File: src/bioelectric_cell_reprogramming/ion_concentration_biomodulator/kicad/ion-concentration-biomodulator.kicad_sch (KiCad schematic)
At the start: 52 parts, among them J1 532610671, J10 39-53-2045, J11 Conn_01x14_Pin, J12 Conn_01x14_Pin, J13 39-53-2045, J14 39-53-2045, J15 Conn_ARM_SWD_TagConnect_TC2030, J16 IPL1-104-01-L-D-K, J17 Conn_01x02_Pin, J18 EJ508A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

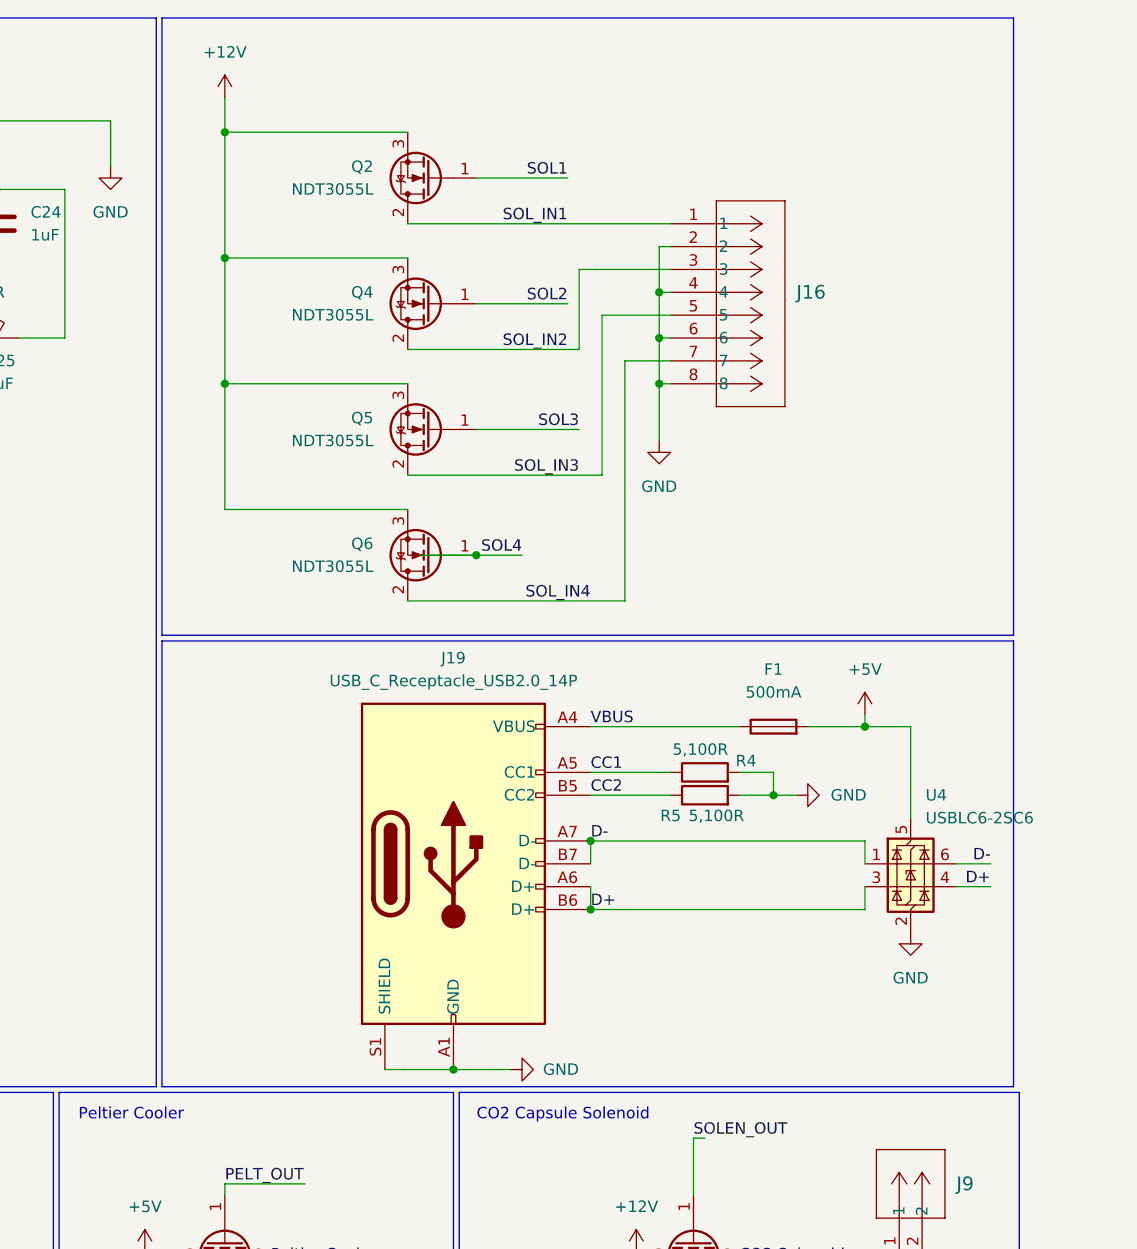
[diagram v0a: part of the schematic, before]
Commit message: fix: replaced the USB connector with one in the JLCPCB parts library
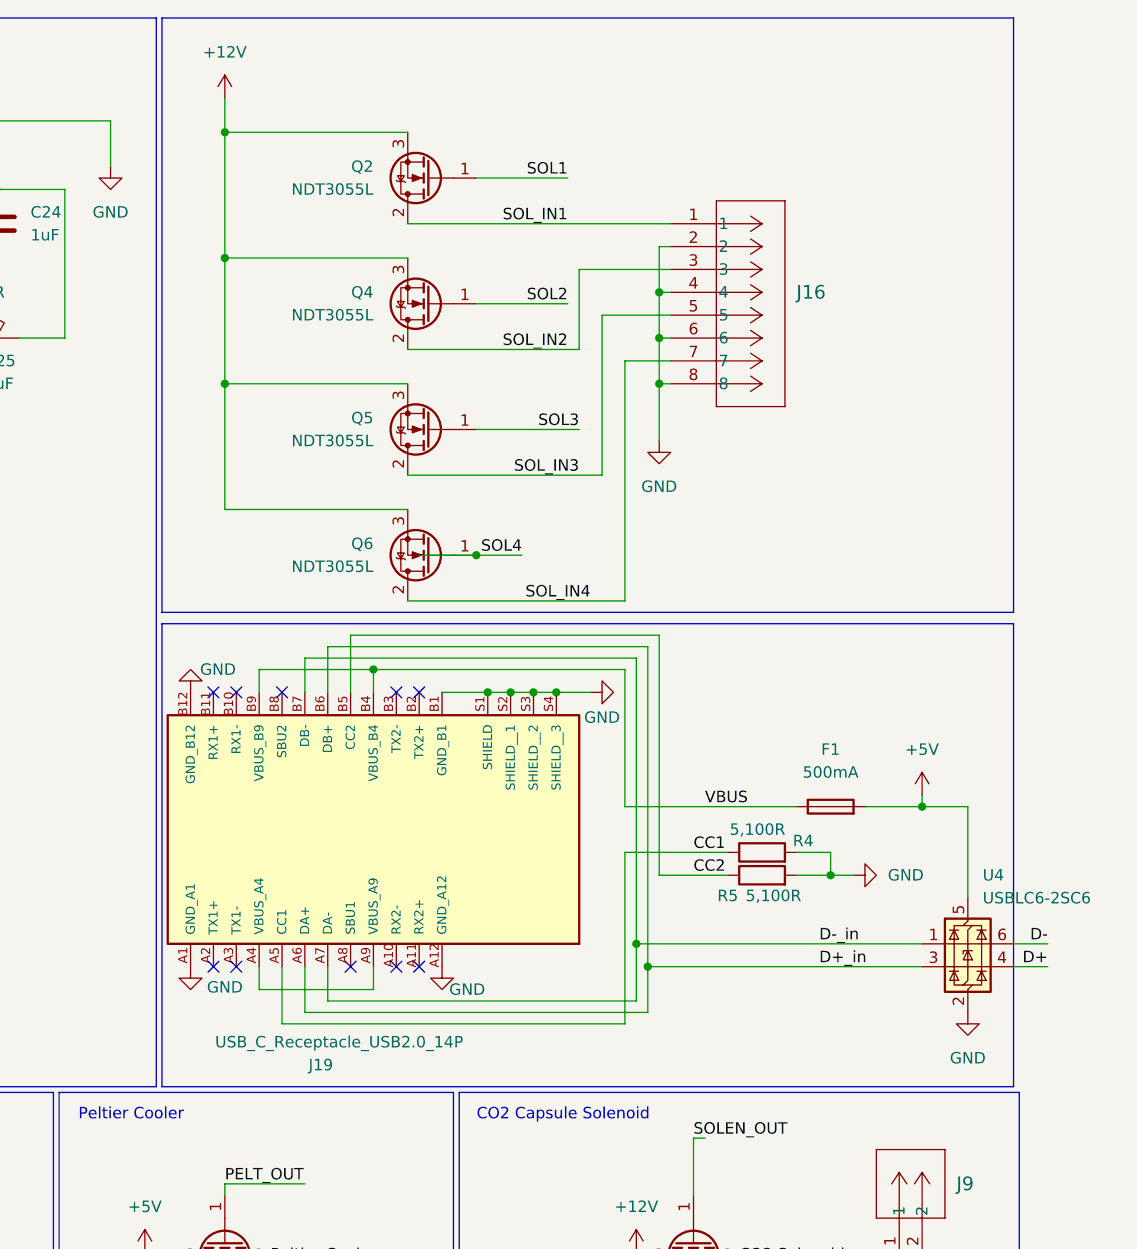
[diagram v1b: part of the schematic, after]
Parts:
- J19: footprint Connector_USB:USB_C_Receptacle_GCT_USB4105-xx-A_16P_TopMnt_Horizontal -> 12401610E4_2A:AMPHENOL_12401610E4_2A; symbol Connector:USB_C_Receptacle_USB2.0_14P -> 12401610E4_2A:12401610E4_2A; MANUFACTURER (none) -> Amphenol; MAXIMUM_PACKAGE_HEIGHT (none) -> 3.43 mm; PARTREV (none) -> C; SNAPEDA_PN (none) -> 12401610E4#2A; STANDARD (none) -> Manufacturer Recommendations
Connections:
- net D+: no longer J19.A6 (D+), J19.B6 (D+), U4.3 (I/O2)
- net D-: no longer J19.A7 (D-), J19.B7 (D-), U4.1 (I/O1)
- net GND: now also J19.S2 (SHIELD__1), J19.S3 (SHIELD__2), J19.S4 (SHIELD__3)
- net VBUS: no longer J19.A4 (VBUS), J19.A9 (VBUS)
- new net: J19.A4 (VBUS_A4), J19.A9 (VBUS_A9)
- new net D+_in: J19.A6 (DA+), J19.B6 (DB+), U4.3 (I/O2)
- new net D-_in: J19.A7 (DA-), J19.B7 (DB-), U4.1 (I/O1)
- no-connect marks 29 -> 39
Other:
- moved on the sheet: F1, R4, R5, U4

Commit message: fix: symbol and footprint libs, and improved routing
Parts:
- removed C16: 1uF, Capacitor_SMD:C_0402_1005Metric, symbol Device:C
- removed C18: 100nF, Capacitor_SMD:C_0402_1005Metric, symbol Device:C
- added C4, C8: 100nF, Capacitor_SMD:C_0201_0603Metric, symbol Device:C
- added C5, C9: 1uF, Capacitor_SMD:C_0201_0603Metric, symbol Device:C
- added J20: 6620XX11122_66200211122, 1x02_socket_66200211122.pretty:66200211122, symbol 6620XX11122_66200211122:6620XX11122_66200211122
- added J21: IPL1-102-01-L-S-K, 1x02_socket_IPL1-102-01-L-S-K.pretty:CONN_IPL1-102-01-L-S-K_SAI, symbol 2024-08-13_01-47-46:IPL1-102-01-L-S-K
- added Q7: NDT3055L, Package_TO_SOT_SMD:SOT-223-3_TabPin2, symbol Transistor_FET:NDT3055L
- added R6: 10K, Resistor_SMD:R_0603_1608Metric, symbol Device:R
- C2, C22, C23, C24, C25, C3: footprint Capacitor_SMD:C_0402_1005Metric -> Capacitor_SMD:C_0201_0603Metric
- C21: value 100nF -> 1uF; footprint Capacitor_SMD:C_0402_1005Metric -> Capacitor_SMD:C_0201_0603Metric
- J1, J2, J3, J4: footprint co2_sensor_footprint:CON_532610671 -> keyed_6_pin_horizontal_0532610671.pretty:CON_532610671; symbol co2_sensor_molex_footprint:532610671 -> 0532610671:532610671
- J10, J13, J14, J8: footprint microfluidics:39532045 -> upright_4_pin_socket_39-53-2045.pretty:39532045; symbol microfluid_connector:39-53-2045 -> 39-53-2045:39-53-2045
- J16: footprint pinch_solenoid:CONN_IPL1-104-01-x-D-x_SAI -> 2x04_socket_IPL1-104-01-L-D-K.pretty:CONN_IPL1-104-01-x-D-x_SAI; symbol 1x08_connector_pinch_solenoid:IPL1-104-01-L-D-K -> 2024-08-13_01-50-37:IPL1-104-01-L-D-K
- J18: footprint barrel_jack_EJ508A:MPD_EJ508A -> Barrel_Jack_EJ508A.pretty:MPD_EJ508A; symbol barrel_jack_EJ508A:EJ508A -> EJ508A:EJ508A
- J19: footprint 12401610E4_2A:AMPHENOL_12401610E4_2A -> 12401610E4_2A.pretty:AMPHENOL_12401610E4_2A
- J5: footprint co2_dev_board_male_socket:CONN4_S4B-PH-SM4-TB_JST -> male_socket_S4B-PH-SM4-TB.pretty:CONN4_S4B-PH-SM4-TB_JST; symbol co2_dev_board_male_socket:S4B-PH-SM4-TB -> 2024-08-13_06-27-45:S4B-PH-SM4-TB
- J7: footprint peltier_cooler_socket_footprint:66200211122 -> 1x02_socket_66200211122.pretty:66200211122; symbol 1x02_connector_peltier:6620XX11122_66200211122 -> 6620XX11122_66200211122:6620XX11122_66200211122
- J9: footprint solenoid_footprint:CONN_IPL1-102-01-L-S-K_SAI -> 1x02_socket_IPL1-102-01-L-S-K.pretty:CONN_IPL1-102-01-L-S-K_SAI; symbol 1x02_connector_solenoid:IPL1-102-01-L-S-K -> 2024-08-13_01-47-46:IPL1-102-01-L-S-K
- R1, R3: value 10,000R -> 10K
- R2: value 220R -> 220
- R4, R5: value 5,100R -> 5K1
- U2: footprint LDO_5V:TS3B -> LDO_5V_LM1084.pretty:TO254P1524X483-4N
- U3: footprint LDO_5V:TS3B -> LDO_3V_LM1084.pretty:TO254P1524X483-4N
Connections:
- net +3.3V: now also C4.1, C5.1, C8.1, C9.1, R6.2
- net +5V: now also Q7.3 (S)
- net 22+: now also J12.8 (Pin_8), J13.2
- net 22-: now also J12.7 (Pin_7), J13.1
- net GND: now also C4.2, C5.2, C8.2, C9.2, J20.2, J21.1
- net SOL2: now also U1.29 (PA8); no longer U1.17 (PA7)
- net VBUS: now also J19.A4 (VBUS_A4), J19.A9 (VBUS_A9)
- net FRIDGE_PELT_OUT: now reaches U1.30 (PA9)
- net FRIDGE_PELT_OUT: now also Q7.1 (G)
- new net Fridge Peltier Cooler: J20.1, Q7.2 (D)
- new net THERM_FEEDBACK: J21.2, R6.1, U1.17 (PA7)
- no-connect marks 39 -> 37
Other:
- note added: "Fridge Peltier Cooler"
- note added: "Fridge Thermistor"
- moved on the sheet: C21, C22, H1, H2, H3, H4, R1, R3

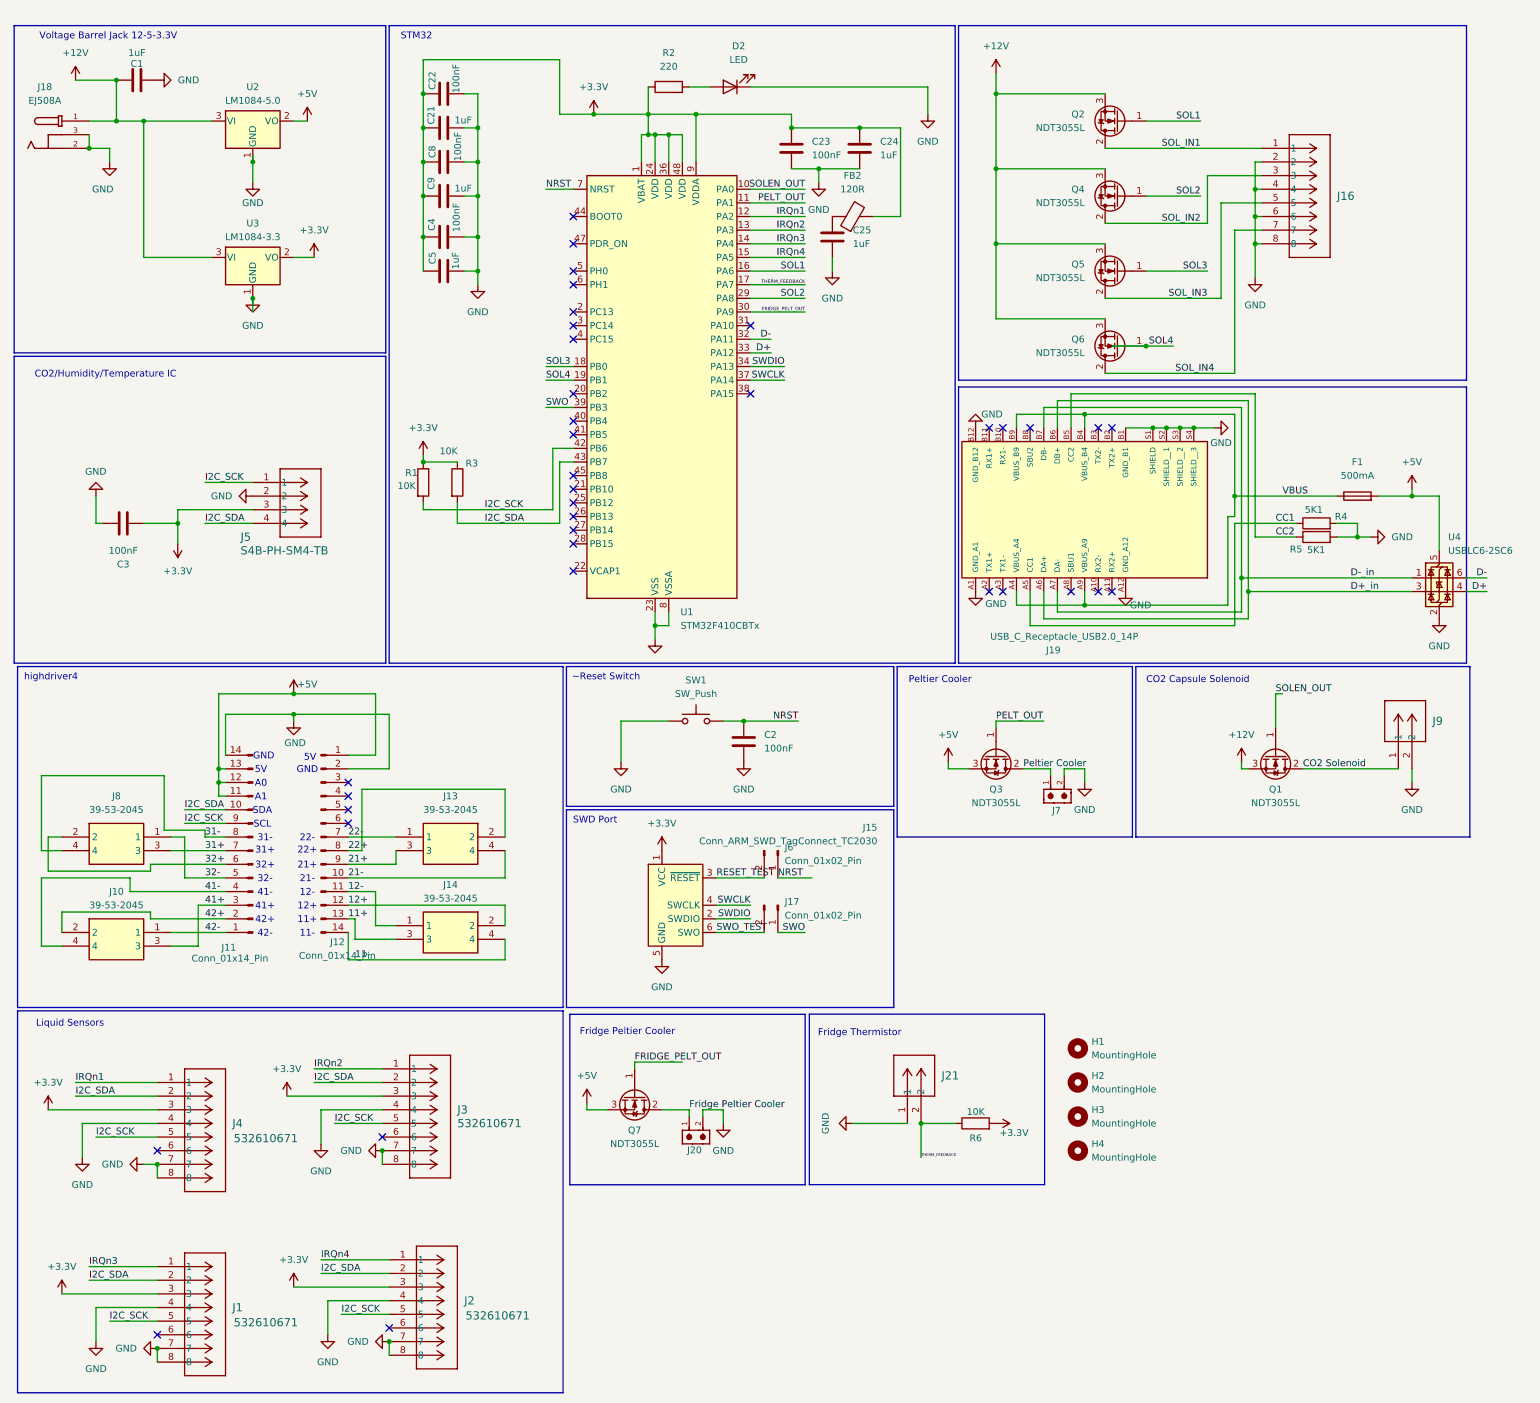
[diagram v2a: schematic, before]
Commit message: fix: move N-channel FETs from high-side to low-side configuration
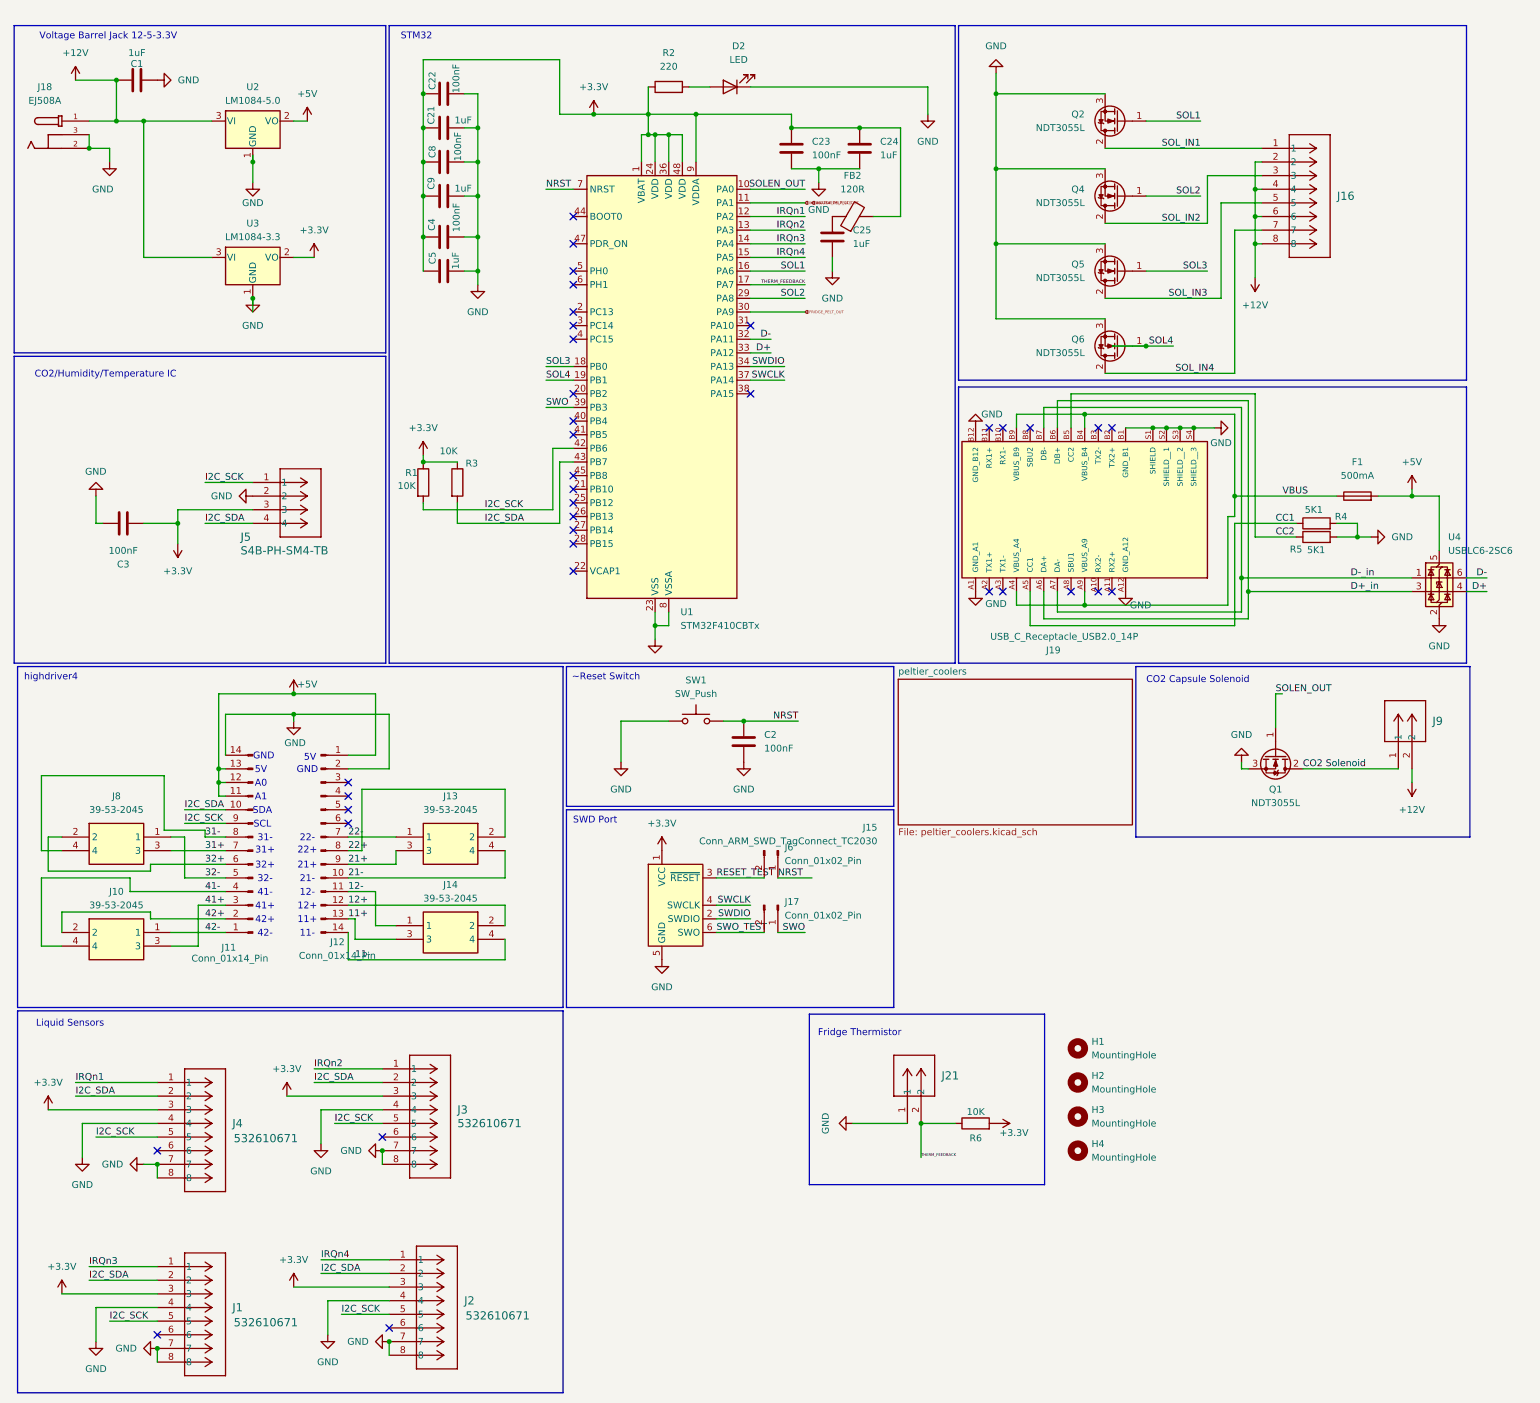
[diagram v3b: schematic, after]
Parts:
- removed J20, J7: 6620XX11122_66200211122, 1x02_socket_66200211122.pretty:66200211122, symbol 6620XX11122_66200211122:6620XX11122_66200211122
- removed Q3, Q7: NDT3055L, Package_TO_SOT_SMD:SOT-223-3_TabPin2, symbol Transistor_FET:NDT3055L
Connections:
- net +12V: now also J16.2, J16.4, J16.6, J16.8, J9.2; no longer Q1.3 (S), Q2.3 (S), Q4.3 (S), Q5.3 (S), Q6.3 (S)
- net GND: now also Q1.3 (S), Q2.3 (S), Q4.3 (S), Q5.3 (S), Q6.3 (S); no longer J16.2, J16.4, J16.6, J16.8, J9.2
- net PELT_OUT renamed INCUBATOR_PELT_OUT
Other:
- added sheet peltier_coolers (peltier_coolers.kicad_sch)
- note removed: "Fridge Peltier Cooler"
- note removed: "Peltier Cooler"
